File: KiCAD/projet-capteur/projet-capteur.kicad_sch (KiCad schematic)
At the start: 15 parts, among them J1 Power, J2 Analog, J3 Digital/PWM, J4 Digital/PWM, U2 LTC1050

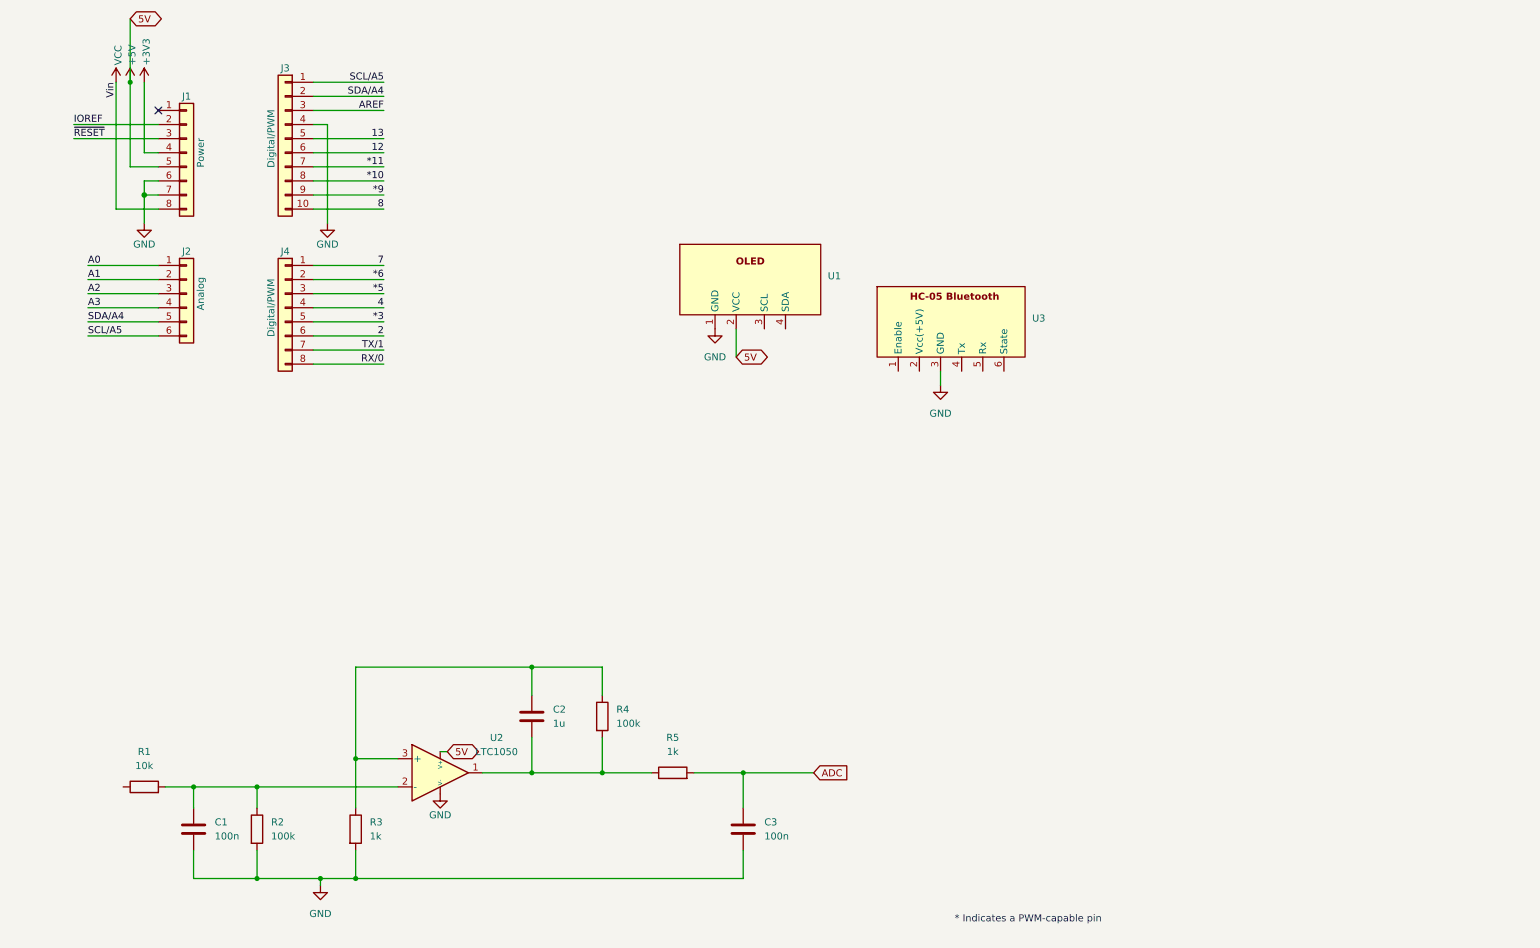
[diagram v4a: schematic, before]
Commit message: pin a jour pour le ltc1050 hc05 connecté
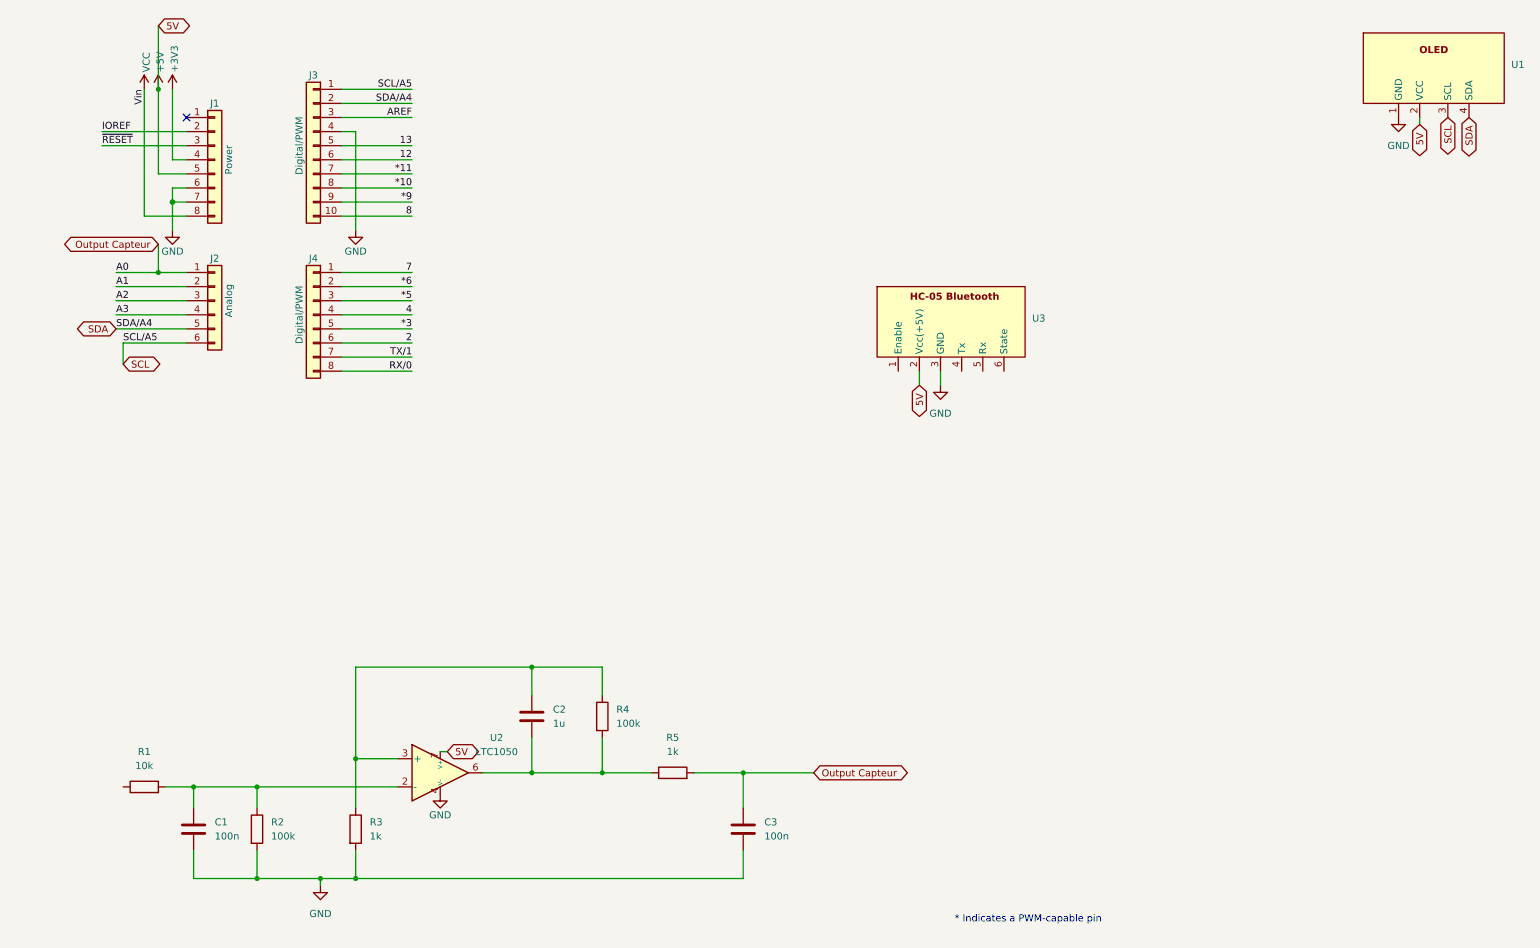
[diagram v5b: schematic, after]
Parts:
- C1, C2, C3: footprint Resistor_THT:R_Axial_DIN0207_L6.3mm_D2.5mm_P5.08mm_Vertical -> Capacitor_THT:C_Disc_D6.0mm_W2.5mm_P5.00mm
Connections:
- net ADC is gone; now on net Output Capteur: C3.1, R5.2
- net SCL/A5 is gone; now on net SCL: J2.6 (Pin_6), J3.1 (Pin_1)
- net SDA/A4 is gone; now on net SDA: J2.5 (Pin_5), J3.2 (Pin_2)
- net +5V: now also U2.7 (V+), U3.2 (Vcc(+5V)); no longer U2. (V-)
- net GND: now also U2.4 (V-); no longer U2. (V-)
- net at C2.2, R4.2, R5.1: now also U2.6; no longer U2.1
- net SCL: now reaches U1.3 (SCL)
- net SDA: now reaches U1.4 (SDA)
- net A0 renamed Output Capteur
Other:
- moved on the sheet: J1, J2, J3, J4, U1

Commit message: Ajout du Flex Sensor et DPotentiometre
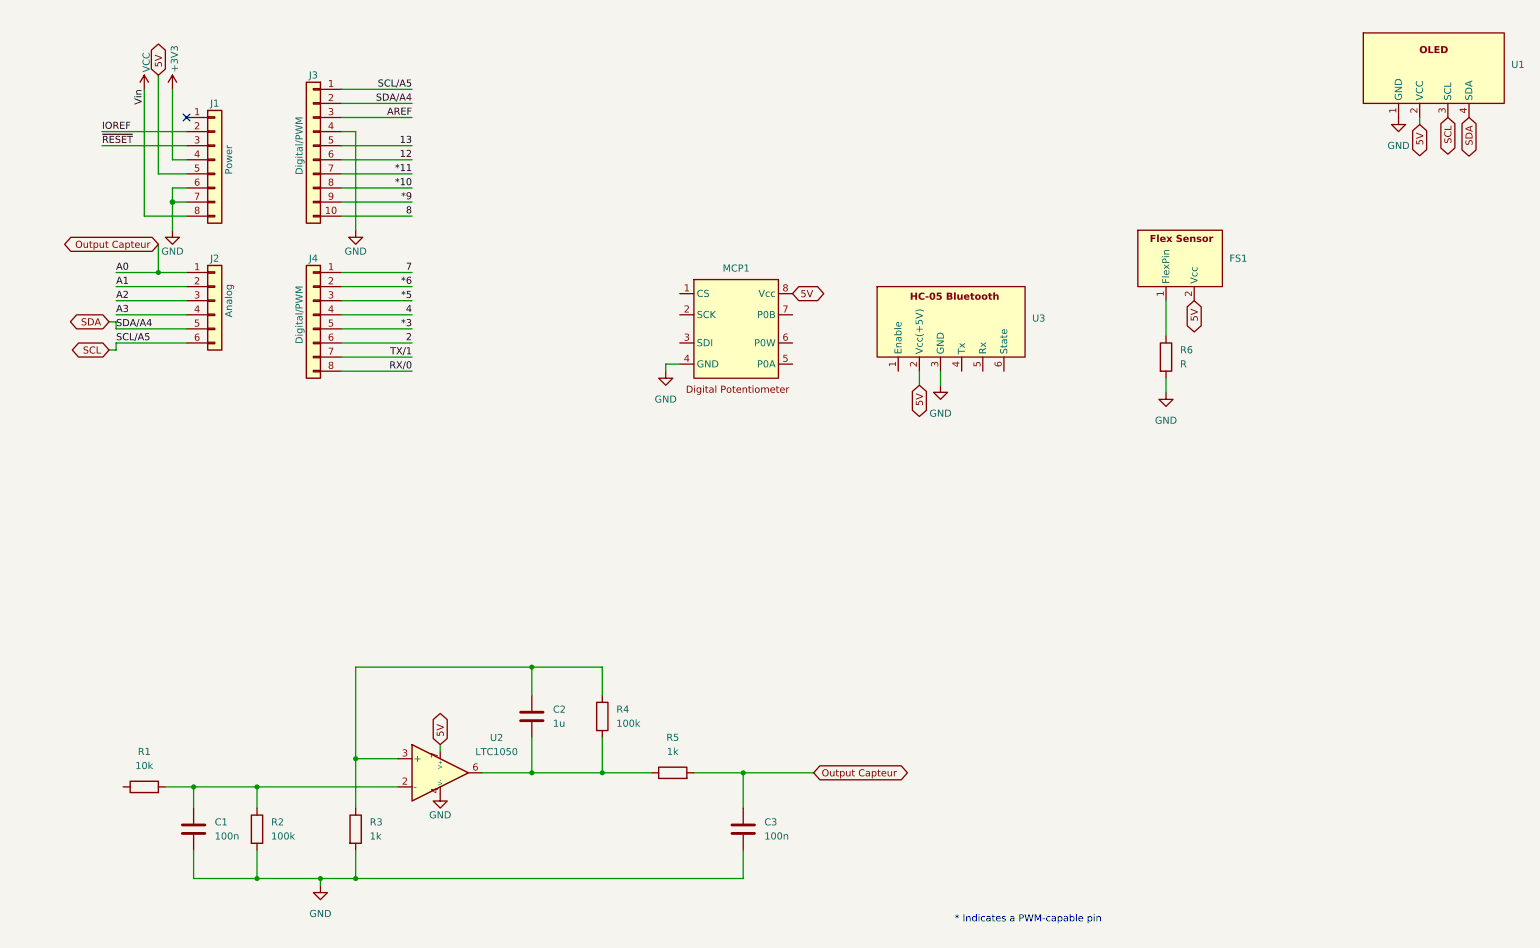
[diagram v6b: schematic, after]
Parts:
- added FS1: ~, MyLibEmpreinte:Flex Sensor, symbol MyLibGraphite:Flex-Sensor
- added MCP1: ~, Package_DIP:DIP-8_W7.62mm, symbol MyLibGraphite:Digital-Potentiometer
- added R6: R, Resistor_THT:R_Axial_DIN0207_L6.3mm_D2.5mm_P5.08mm_Vertical, symbol Device:R
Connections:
- net GND: now also MCP1.4 (GND), R6.2
- net +5V renamed 5V
- net 5V: now also FS1.2 (Vcc), MCP1.8 (Vcc)
- new net: FS1.1 (FlexPin), R6.1

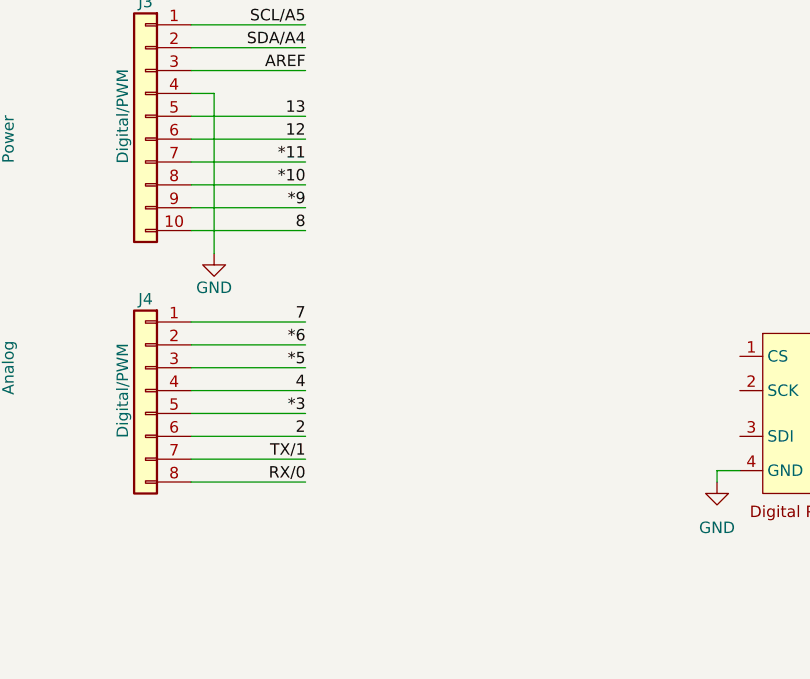
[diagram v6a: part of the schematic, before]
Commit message: Ajout du header Servo Moteur
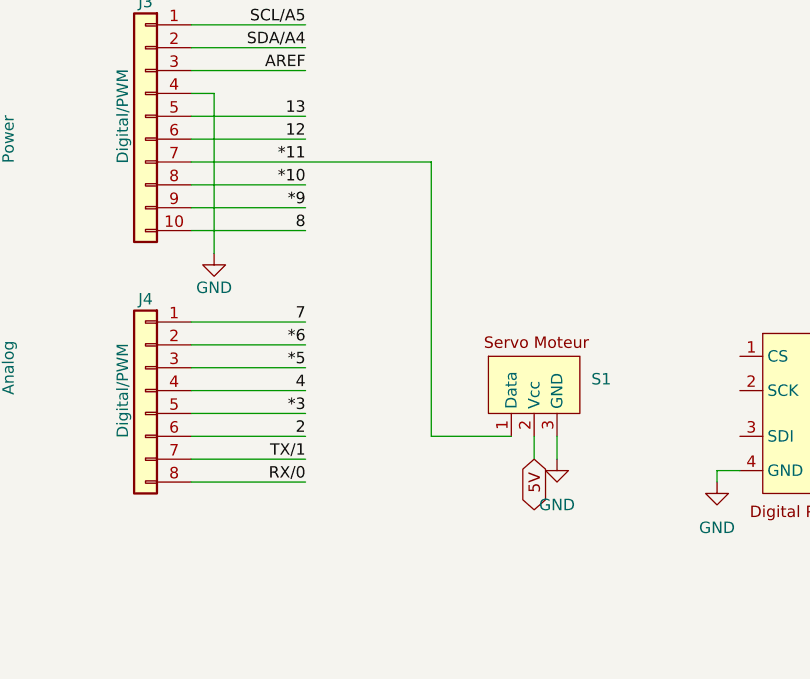
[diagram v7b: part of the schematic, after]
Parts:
- added S1: ~, MyLibEmpreinte:ServoMoteur, symbol MyLibGraphite:Servo
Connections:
- net *11: now also S1.1 (Data)
- net 5V: now also S1.2 (Vcc)
- net GND: now also S1.3 (GND)
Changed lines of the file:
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@@
+	(wire
+		(pts
+			(xy 93.98 73.66) (xy 93.98 43.18)
+		)
+		(stroke
+			(width 0)
+			(type default)
+		)
+	)
 	(wire
 		(pts
@@
 	(wire
 		(pts
+			(xy 102.87 73.66) (xy 93.98 73.66)
+		)
+		(stroke
+			(width 0)
+			(type default)
+		)
+	)
+	(wire
+		(pts
 			(xy 101.6 132.08) (xy 101.6 137.16)
 		)
@@
 	(wire
 		(pts
-			(xy 67.31 43.18) (xy 80.01 43.18)
+			(xy 67.31 43.18) (xy 93.98 43.18)
 		)
 		(stroke
@@
 	(wire
 		(pts
+			(xy 107.95 76.2) (xy 107.95 73.66)
+		)
+		(stroke
+			(width 0)
+			(type default)
+		)
+	)
+	(wire
+		(pts
 			(xy 175.26 78.74) (xy 175.26 81.28)
 		)
@@
 			(width 0)
 			(type solid)
+		)
+	)
+	(wire
+		(pts
+			(xy 105.41 76.2) (xy 105.41 73.66)
+		)
+		(stroke
+			(width 0)
+			(type default)
 		)
 	)
@@
 		(property "Intersheetrefs" "${INTERSHEET_REFS}"
 			(at 15.6797 55.88 0)
+			(effects
+				(font
+					(size 1.27 1.27)
+				)
+				(justify right)
+				(hide yes)
+			)
+		)
+	)
+	(global_label "5V"
+		(shape bidirectional)
+		(at 105.41 76.2 270)
+		(fields_autoplaced yes)
+		(effects
+			(font
+				(size 1.27 1.27)
+			)
+			(justify right)
+		)
+		(property "Intersheetrefs" "${INTERSHEET_REFS}"
+			(at 105.41 82.5944 90)
 			(effects
 				(font
@@
 	)
 	(symbol
+		(lib_name "GND_2")
+		(lib_id "power:GND")
+		(at 107.95 76.2 0)
+		(unit 1)
+		(exclude_from_sim no)
+		(in_bom yes)
+		(on_board yes)
+		(dnp no)
+		(fields_autoplaced yes)
+		(property "Reference" "#PWR05"
+			(at 107.95 82.55 0)
+			(effects
+				(font
+					(size 1.27 1.27)
+				)
+				(hide yes)
+			)
+		)
+		(property "Value" "GND"
+			(at 107.95 81.28 0)
+			(effects
+				(font
+					(size 1.27 1.27)
+				)
+			)
+		)
+		(property "Footprint" ""
+			(at 107.95 76.2 0)
+			(effects
+				(font
+					(size 1.27 1.27)
+				)
+				(hide yes)
+			)
+		)
+		(property "Datasheet" ""
+			(at 107.95 76.2 0)
+			(effects
+				(font
+					(size 1.27 1.27)
+				)
+				(hide yes)
+			)
+		)
+		(property "Description" "Power symbol creates a global label with name \"GND\" , ground"
+			(at 107.95 76.2 0)
+			(effects
+				(font
+					(size 1.27 1.27)
+				)
+				(hide yes)
+			)
+		)
+		(pin "1"
+		)
+		(instances
+			(project "projet-capteur"
+				(path "/e63e39d7-6ac0-4ffd-8aa3-1841a4541b55"
+					(reference "#PWR05")
+					(unit 1)
+				)
+			)
+		)
+	)
+	(symbol
 		(lib_id "Device:R")
 		(at 127 151.13 90)
@@
 					(unit 1)
 				)
+			)
+		)
+	)
+	(symbol
+		(lib_id "MyLibGraphite:Servo")
+		(at 105.41 63.5 0)
+		(unit 1)
+		(exclude_from_sim no)
+		(in_bom yes)
+		(on_board yes)
+		(dnp no)
+		(fields_autoplaced yes)
+		(property "Reference" "S1"
+			(at 111.76 67.3099 0)
+			(effects
+				(font
+					(size 1.27 1.27)
+				)
+				(justify left)
+			)
+		)
+		(property "Value" "~"
+			(at 111.76 69.215 0)
+			(effects
+				(font
+					(size 1.27 1.27)
+				)
+				(justify left)
+			)
+		)
+		(property "Footprint" "MyLibEmpreinte:ServoMoteur"
+			(at 105.41 63.5 0)
+			(effects
+				(font
+					(size 1.27 1.27)
+				)
+				(hide yes)
+			)
+		)
+		(property "Datasheet" ""
+			(at 105.41 63.5 0)
+			(effects
+				(font
+					(size 1.27 1.27)
+				)
+				(hide yes)
+			)
+		)
+		(property "Description" ""
+			(at 105.41 63.5 0)
+			(effects
+				(font
+					(size 1.27 1.27)
+				)
+				(hide yes)
+			)
+		)
+		(pin "1"
+		)
+		(pin "2"
+		)
+		(pin "3"
+		)
+		(instances
+			(project ""
+				(path "/e63e39d7-6ac0-4ffd-8aa3-1841a4541b55"
+					(reference "S1")
+					(unit 1)
+				)

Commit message: Seance Realisation du shield 12.03
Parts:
- added ROE1: ~, MyLibEmpreinte:Rotary Encoder, symbol MyLibGraphite:Rotary_Encoder
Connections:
- net *10: now also MCP1.1 (CS)
- net *11: now also MCP1.3 (SDI); no longer S1.1 (Data)
- net *3: now also U3.4 (Tx)
- net *9: now also S1.1 (Data)
- net 13: now also MCP1.2 (SCK)
- net 2: now also U3.5 (Rx)
- net Sortie Capteur: now reaches R1.1
- net Output Capteur renamed ADC
- no-connect marks 1 -> 3
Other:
- moved on the sheet: J2, J4, S1, U3
